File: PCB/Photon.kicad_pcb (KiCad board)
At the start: 2 copper layers, 21.2 x 74.4 mm, 43 parts, among them J1 USB_C_Receptacle_USB2.0_14P, J2 Conn_01x05_Socket, Q1 IRLML6402, Q2 IRLML6402, SW1 TS-1088-AR02016, U1 PY32F002AL15S6TU, U2 TP4056, U3 RT8059GJ5, U4 BCR421UW6-7, U5 DW01A, U6 FS8205A, U7 BCR421UW6-7

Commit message: Squashed commit of the following:
commit 040f56c92c5fbfa60c6357d084ca9e817f85bd74
Author: AirMatress <134566567+Kay-Jack@users.noreply.github.com>
Date:   Sun Feb 15 22:31:25 2026 -0500

    changed folder structure and added new photos

commit a5de8e0470fd1fbaa1884b4c13b8efd9701bd3f9
Author: AirMatress <134566567+Kay-Jack@users.noreply.github.com>
Date:   Sun Feb 15 22:04:27 2026 -0500

    added zip

commit 86241a126469fe2acf0b48b8ae5ce0ab9d585c9c
Author: AirMatress <134566567+Kay-Jack@users.noreply.github.com>
Date:   Sun Feb 15 21:56:49 2026 -0500

    added gerbers

commit 35698b9b92e03ab22e12582723e18a858d02b47b
Author: AirMatress <134566567+Kay-Jack@users.noreply.github.com>
Date:   Sun Feb 15 21:54:39 2026 -0500

    switch to smt32 mcu and cleaned up pcb

commit b81d1645440da80b902de656f60b2bd3905a4b55
Author: AirMatress <134566567+Kay-Jack@users.noreply.github.com>
Date:   Sun Jan 18 22:33:01 2026 -0500

    updated debug header and changed resistors for UVLO

    Applied teardrop to all vias. some were missing. Thickened trace from neg battery terminal. Updated gerbers

commit b8795243000142daf8d6161322fd58468c0a1805
Author: AirMatress <134566567+Kay-Jack@users.noreply.github.com>
Date:   Mon Jan 5 22:00:06 2026 -0500

    Rotated PCB

commit 89b92c6a3bacb1a8dd3ef43ffdd3007030cc7a51
Author: AirMatress <134566567+Kay-Jack@users.noreply.github.com>
Date:   Mon Jan 5 21:30:51 2026 -0500

    updated photos and added path for step of tp4056

commit 6c3586d8c21dee7771f43999eac4c35423b5389e
Author: AirMatress <134566567+AirMatress@users.noreply.github.com>
Date:   Thu Jan 1 13:02:22 2026 -0500

    added UVLO for the buck
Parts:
- added C2: 100nF, Capacitor_SMD:C_0603_1608Metric, F.Cu at (54.2, 67.2)
- added R5: 12K, Resistor_SMD:R_0603_1608Metric, F.Cu at (52.4, 61.2)
- C1: value 100nF -> 4.7uF; footprint Capacitor_SMD:C_0603_1608Metric -> Capacitor_SMD:C_0805_2012Metric
- J1: value USB_C_Receptacle_USB2.0_14P -> USB_C_Receptacle_USB2.0_6P
- R6: value 100K -> 10K
- U1: value PY32F002AL15S6TU -> STM32G030F6P6TR; footprint Package_SO:SOP-8_3.9x4.9mm_P1.27mm -> Package_SO:TSSOP-20_4.4x6.5mm_P0.65mm
- U2: footprint Package_SO:SOIC-8-1EP_3.9x4.9mm_P1.27mm_EP2.29x3mm -> Package_SO:SOIC-8-1EP_3.9x4.9mm_P1.27mm_EP2.41x3.3mm
- moved BT1 4.73 mm to (43.9, 37.3)
- moved C3 4.73 mm to (42.0, 34.5)
- moved C6 4.73 mm to (45.1, 60.4)
- moved C8 4.73 mm to (43.4, 90.7)
- moved G*** 4.73 mm to (56.8, 83.0)
- moved J2 4.73 mm to (41.0, 72.3)
- moved L1 4.73 mm to (53.5, 57.2)
- moved R10 4.73 mm to (48.4, 62.2)
- moved R11 4.73 mm to (43.4, 87.3)
- moved R13 4.73 mm to (49.4, 87.3)
- moved R14 4.73 mm to (55.5, 90.7)
- moved R8 4.73 mm to (42.0, 36.0)
- moved R9 4.73 mm to (45.1, 62.2)
- moved U4 4.73 mm to (46.8, 90.7)
- moved U5 4.73 mm to (52.2, 90.7)
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- renumbered C2 to C4, C6 to C5, C4 to C6, C5 to C7, C7 to C8, R9 to R10, R14 to R11, R13 to R12, R17 to R13, R19 to R14, R16 to R15, R7 to R3, R10 to R4, R4 to R7, R5 to R8, R8 to R9, U5 to U4, U6 to U5, U4 to U6
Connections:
- net /NRST renamed NRST
- J2 pad 1: GND -> +3V3
- J2 pad 2: /SWC -> SWCLK
- J2 pad 3: /SWD -> SWDIO
- J2 pad 5: +3V3 -> GND
- R6 pad 1: /VBAT_SYS -> /UVLO
- SW1 pad 1: /BTN -> /BUTN
- U1 pad 1: +3V3 -> unconnected-(U1-PB7/PB8-Pad1)
- U1 pad 2: /LED1_EN -> unconnected-(U1-PB9/PC14-Pad2)
- U1 pad 3: /LED2_EN -> unconnected-(U1-PC15-Pad3)
- U1 pad 4: /SWC -> +3V3
- U1 pad 5: /SWD -> GND
- U1 pad 7: /BTN -> unconnected-(U1-PA0-Pad7)
- U1 pad 8: GND -> unconnected-(U1-PA1-Pad8)
- U3 pad 1: /VBAT_SYS -> /UVLO
- U6 pad 1: /LED1_EN -> LED1_EN
- U7 pad 1: /LED2_EN -> LED2_EN
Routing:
- net /LED1_EN: track 32.3 -> 0.00 mm, vias 2 -> 0
- net /BUTN: track 0.00 -> 26.3 mm, vias 0 -> 2
- net /BTN: track 23.9 -> 0.00 mm, vias 2 -> 0
- net LED1_EN: track 0.00 -> 23.3 mm, vias 0 -> 2
- net /LED2_EN: track 19.3 -> 0.00 mm, vias 2 -> 0
- net LED2_EN: track 0.00 -> 18.1 mm, vias 0 -> 4
- net /SWC: track 12.8 -> 0.00 mm, vias 1 -> 0
- net /SWD: track 8.80 -> 0.00 mm, vias 1 -> 0
- net NRST: track 4.66 -> 11.7 mm
- net +3V3: track 65.0 -> 70.9 mm, vias 3 -> 4
- net SWDIO: track 0.00 -> 5.90 mm, vias 0 -> 1
- net SWCLK: track 0.00 -> 5.37 mm, vias 0 -> 1
- net /UVLO: track 0.00 -> 3.86 mm
- net /DSBL: track 9.26 -> 10.8 mm
- net GND: track 0.00 -> 1.38 mm, vias 52 -> 39
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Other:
- board text added: "V6 02-15-2026"
- board text removed: "V5"

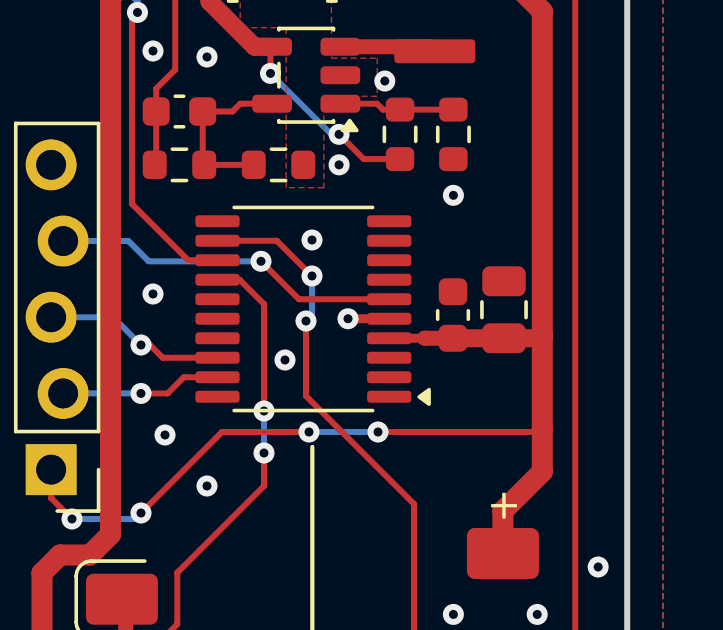
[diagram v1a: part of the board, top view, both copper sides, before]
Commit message: caps too close, resolved and updated gerbers
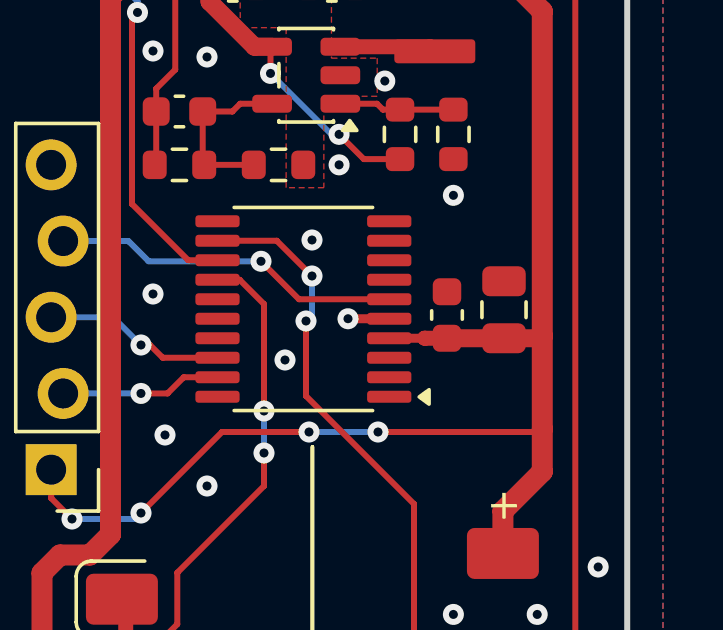
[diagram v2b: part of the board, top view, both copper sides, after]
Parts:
- moved C2 0.20 mm to (54.0, 67.2)
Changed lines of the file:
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@@
 	(footprint "Capacitor_SMD:C_0603_1608Metric"
 		(layer "F.Cu")
-		(at 54.2 67.175 90)
+		(at 54 67.175 90)
 		(descr "Capacitor SMD 0603 (1608 Metric), square (rectangular) end terminal, IPC-7351 nominal, (Body size source: IPC-SM-782 page 76, https://www.pcb-3d.com/wordpress/wp-content/uploads/ipc-sm-782a_amendment_1_and_2.pdf), generated with kicad-footprint-generator")
 		(tags "capacitor")
